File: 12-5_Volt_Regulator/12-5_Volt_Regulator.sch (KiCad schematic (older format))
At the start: 21 parts, among them J1 Conn_01x02, J2 Conn_01x02, U1 LM22676MR-5

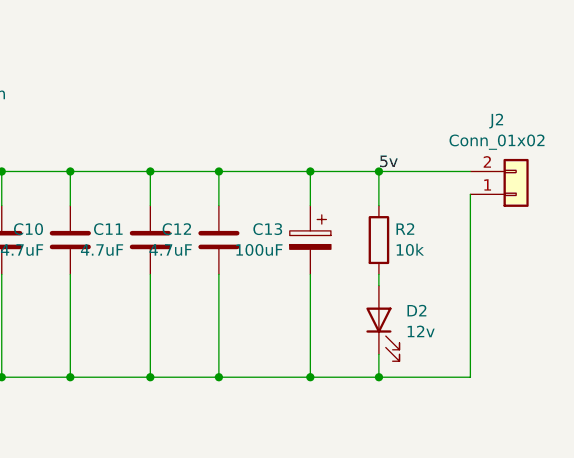
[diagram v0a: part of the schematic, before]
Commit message: Added wire pads, removed vias & fills as I switched grid spacing
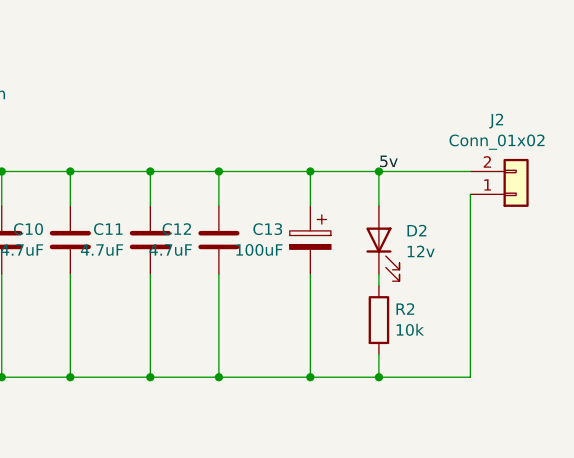
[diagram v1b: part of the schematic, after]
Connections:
- net 5v: now also D2.2 (A); no longer R2.1
- net GND: now also R2.2; no longer D2.1 (K)
- new net: D2.1 (K), R2.1
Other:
- moved on the sheet: D2, R2
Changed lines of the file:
@@
 L Device:R R2
 U 1 1 60F851D1
-P 8700 3500
-F 0 "R2" H 8770 3546 50  0000 L CNN
-F 1 "10k" H 8770 3455 50  0000 L CNN
-F 2 "Resistor_SMD:R_0805_2012Metric" V 8630 3500 50  0001 C CNN
-F 3 "~" H 8700 3500 50  0001 C CNN
-	1    8700 3500
+P 8700 3850
+F 0 "R2" H 8770 3896 50  0000 L CNN
+F 1 "10k" H 8770 3805 50  0000 L CNN
+F 2 "Resistor_SMD:R_0805_2012Metric" V 8630 3850 50  0001 C CNN
+F 3 "~" H 8700 3850 50  0001 C CNN
+	1    8700 3850
 	1    0    0    -1
 $EndComp
@@
 L Device:LED D2
 U 1 1 60F851D7
-P 8700 3850
-F 0 "D2" V 8739 3732 50  0000 R CNN
-F 1 "12v" V 8648 3732 50  0000 R CNN
-F 2 "LED_THT:LED_D3.0mm" H 8700 3850 50  0001 C CNN
-F 3 "~" H 8700 3850 50  0001 C CNN
-	1    8700 3850
+P 8700 3500
+F 0 "D2" V 8739 3382 50  0000 R CNN
+F 1 "12v" V 8648 3382 50  0000 R CNN
+F 2 "LED_THT:LED_D3.0mm" H 8700 3500 50  0001 C CNN
+F 3 "~" H 8700 3500 50  0001 C CNN
+	1    8700 3500
 	0    -1   -1   0
 $EndComp
